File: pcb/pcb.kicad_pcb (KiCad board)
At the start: 2 copper layers, 21 x 51.1 mm, 37 parts, among them J1 USB_C_Receptacle_USB2.0_14P, J2 Conn_01x20, J3 Conn_01x20, J4 Conn_01x03, SW1 SW_Push, U1 RP2040, U2 MCP1700x-330xxTT, U3 W25Q16JVZPIQ, Y1 12 MHz

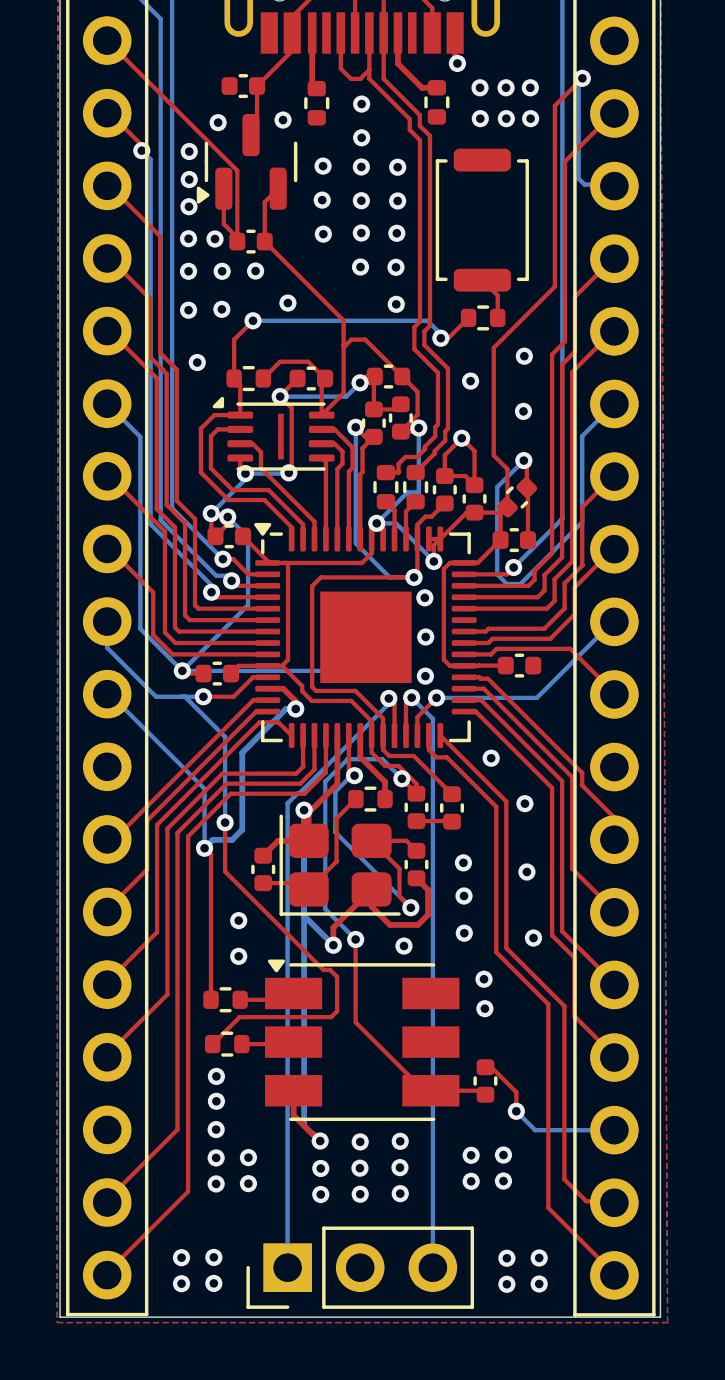
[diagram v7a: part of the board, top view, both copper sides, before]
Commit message: added silkscreen
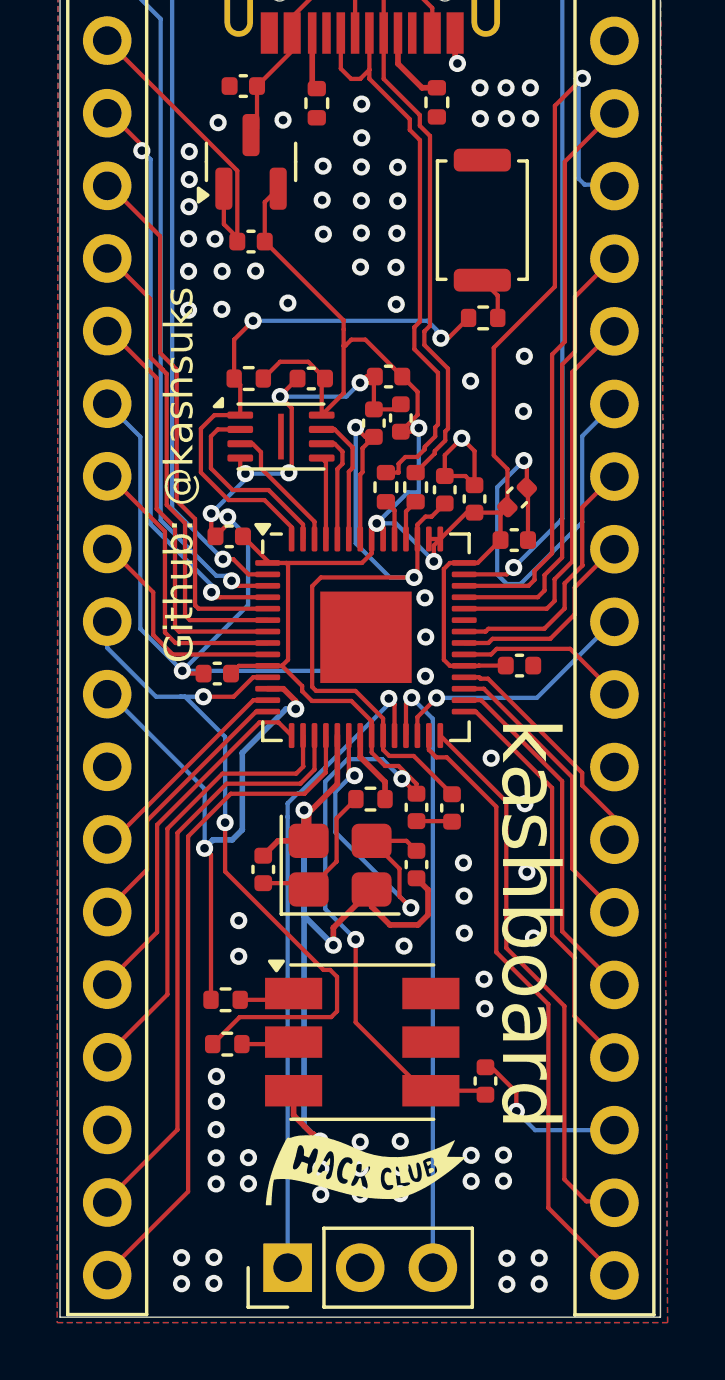
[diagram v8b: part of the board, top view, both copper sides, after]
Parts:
- added G***: LOGO, LOGO, F.Cu at (101.5, 110.7)
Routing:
- net GND: vias 99 -> 98
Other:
- board text added: "Github: @kashsuks"
- board text added: "kashboard"
